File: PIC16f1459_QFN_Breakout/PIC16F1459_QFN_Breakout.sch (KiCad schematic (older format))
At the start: 9 parts, among them P1 CONN_01X05, P2 USB_OTG, P3 CONN_01X08, P4 CONN_01X08, U1 16F1459_QFN20

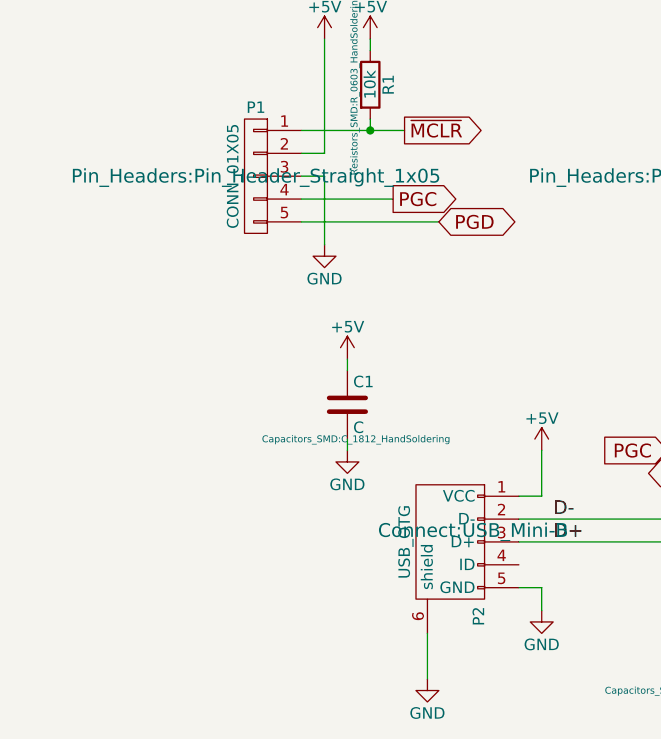
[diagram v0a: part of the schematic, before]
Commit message: Updated PIC16 breakout
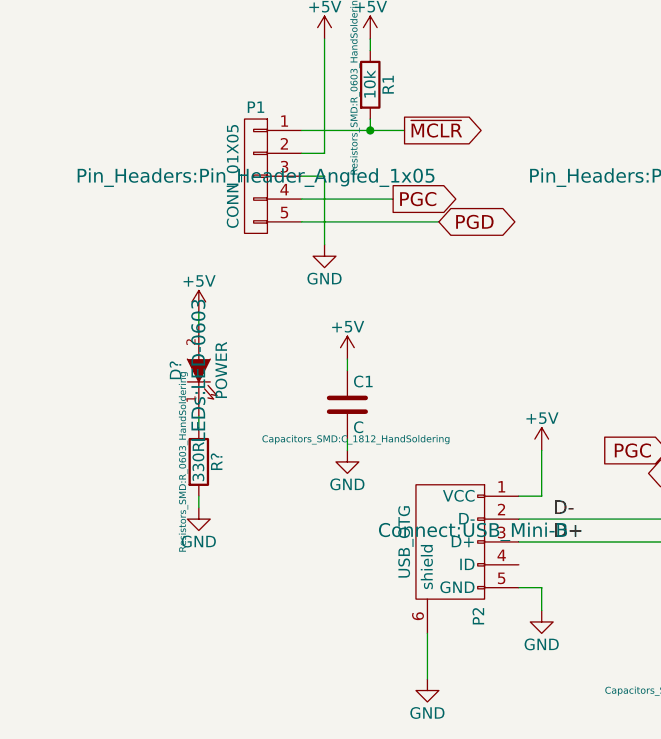
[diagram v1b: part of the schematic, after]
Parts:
- added D?: POWER, LEDs:LED-0603, symbol LED
- added R?: 330R, Resistors_SMD:R_0603_HandSoldering, symbol R
- P1: footprint Pin_Headers:Pin_Header_Straight_1x05 -> Pin_Headers:Pin_Header_Angled_1x05
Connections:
- net +5V: now also D?.2 (A)
- net GND: now also R?.2
- new net: D?.1 (K), R?.1
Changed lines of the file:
@@
 F 0 "P1" H 1050 1750 50  0000 C CNN
 F 1 "CONN_01X05" V 1150 1450 50  0000 C CNN
-F 2 "Pin_Headers:Pin_Header_Straight_1x05" H 1050 1450 60  0000 C CNN
+F 2 "Pin_Headers:Pin_Header_Angled_1x05" H 1050 1450 60  0000 C CNN
 F 3 "" H 1050 1450 60  0000 C CNN
 	1    1050 1450
@@
 Wire Wire Line
 	5450 2550 5450 1300
+$Comp
+L R R?
+U 1 1 565B9800
+P 800 2700
+F 0 "R?" V 880 2700 50  0000 C CNN
+F 1 "330R" V 800 2700 50  0000 C CNN
+F 2 "Resistors_SMD:R_0603_HandSoldering" V 730 2700 30  0000 C CNN
+F 3 "" H 800 2700 30  0000 C CNN
+	1    800  2700
+	1    0    0    -1
+$EndComp
+$Comp
+L GND #PWR?
+U 1 1 565B9870
+P 800 2900
+F 0 "#PWR?" H 800 2650 50  0001 C CNN
+F 1 "GND" H 800 2750 50  0000 C CNN
+F 2 "" H 800 2900 60  0000 C CNN
+F 3 "" H 800 2900 60  0000 C CNN
+	1    800  2900
+	1    0    0    -1
+$EndComp
+$Comp
+L +5V #PWR?
+U 1 1 565B9899
+P 800 2050
+F 0 "#PWR?" H 800 1900 50  0001 C CNN
+F 1 "+5V" H 800 2190 50  0000 C CNN
+F 2 "" H 800 2050 60  0000 C CNN
+F 3 "" H 800 2050 60  0000 C CNN
+	1    800  2050
+	1    0    0    -1
+$EndComp
+$Comp
+L LED D?
+U 1 1 565B98BA
+P 800 2300
+F 0 "D?" H 800 2400 50  0000 C CNN
+F 1 "POWER" H 800 2200 50  0000 C CNN
+F 2 "LEDs:LED-0603" H 800 2300 60  0000 C CNN
+F 3 "" H 800 2300 60  0000 C CNN
+	1    800  2300
+	0    -1   -1   0
+$EndComp
+Wire Wire Line
+	800  2900 800  2850
+Wire Wire Line
+	800  2550 800  2500
+Wire Wire Line
+	800  2100 800  2050
 $EndSCHEMATC

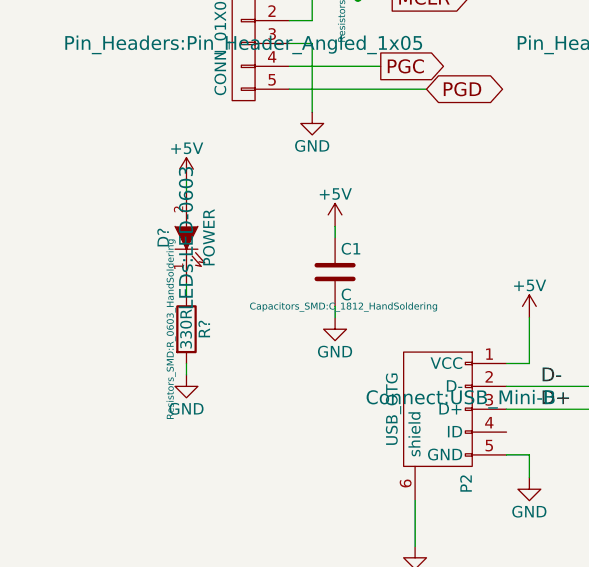
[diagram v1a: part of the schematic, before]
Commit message: Updated PIC16 breakout
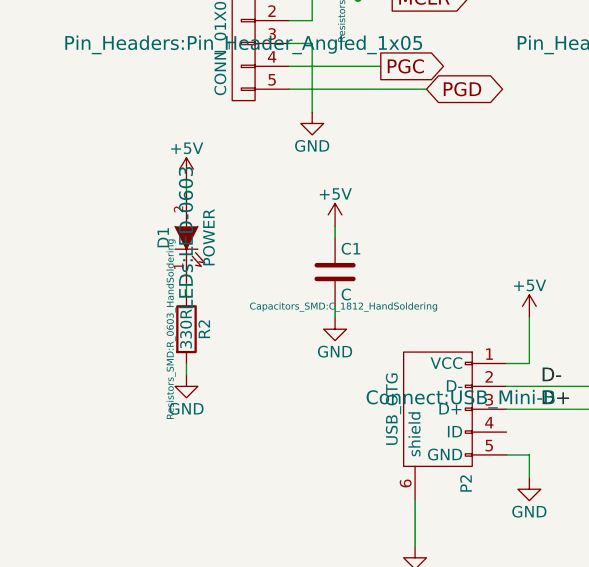
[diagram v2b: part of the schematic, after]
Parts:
- gave numbers to parts that had none: 2
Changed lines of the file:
@@
 $EndComp
 $Comp
-L GND #PWR01
+L GND #PWR10
 U 1 1 565AF913
 P 2300 3350
-F 0 "#PWR01" H 2300 3100 50  0001 C CNN
+F 0 "#PWR10" H 2300 3100 50  0001 C CNN
 F 1 "GND" H 2300 3200 50  0000 C CNN
 F 2 "" H 2300 3350 60  0000 C CNN
@@
 $EndComp
 $Comp
-L GND #PWR02
+L GND #PWR8
 U 1 1 565AF928
 P 1800 3650
-F 0 "#PWR02" H 1800 3400 50  0001 C CNN
+F 0 "#PWR8" H 1800 3400 50  0001 C CNN
 F 1 "GND" H 1800 3500 50  0000 C CNN
 F 2 "" H 1800 3650 60  0000 C CNN
@@
 $EndComp
 $Comp
-L +5V #PWR03
+L +5V #PWR9
 U 1 1 565AF95A
 P 2300 2650
-F 0 "#PWR03" H 2300 2500 50  0001 C CNN
+F 0 "#PWR9" H 2300 2500 50  0001 C CNN
 F 1 "+5V" H 2300 2790 50  0000 C CNN
 F 2 "" H 2300 2650 60  0000 C CNN
@@
 $EndComp
 $Comp
-L +5V #PWR04
+L +5V #PWR5
 U 1 1 565AF970
 P 1450 2250
-F 0 "#PWR04" H 1450 2100 50  0001 C CNN
+F 0 "#PWR5" H 1450 2100 50  0001 C CNN
 F 1 "+5V" H 1450 2390 50  0000 C CNN
 F 2 "" H 1450 2250 60  0000 C CNN
@@
 $EndComp
 $Comp
-L GND #PWR05
+L GND #PWR6
 U 1 1 565AF97E
 P 1450 2650
-F 0 "#PWR05" H 1450 2400 50  0001 C CNN
+F 0 "#PWR6" H 1450 2400 50  0001 C CNN
 F 1 "GND" H 1450 2500 50  0000 C CNN
 F 2 "" H 1450 2650 60  0000 C CNN
@@
 $EndComp
 $Comp
-L +5V #PWR06
+L +5V #PWR3
 U 1 1 565AFBB5
 P 1350 850
-F 0 "#PWR06" H 1350 700 50  0001 C CNN
+F 0 "#PWR3" H 1350 700 50  0001 C CNN
 F 1 "+5V" H 1350 990 50  0000 C CNN
 F 2 "" H 1350 850 60  0000 C CNN
@@
 $EndComp
 $Comp
-L GND #PWR07
+L GND #PWR4
 U 1 1 565AFBDC
 P 1350 1750
-F 0 "#PWR07" H 1350 1500 50  0001 C CNN
+F 0 "#PWR4" H 1350 1500 50  0001 C CNN
 F 1 "GND" H 1350 1600 50  0000 C CNN
 F 2 "" H 1350 1750 60  0000 C CNN
@@
 ~MCLR
 $Comp
-L +5V #PWR08
+L +5V #PWR7
 U 1 1 565AFC9F
 P 1550 850
-F 0 "#PWR08" H 1550 700 50  0001 C CNN
+F 0 "#PWR7" H 1550 700 50  0001 C CNN
 F 1 "+5V" H 1550 990 50  0000 C CNN
 F 2 "" H 1550 850 60  0000 C CNN
@@
 $EndComp
 $Comp
-L GND #PWR09
+L GND #PWR11
 U 1 1 565B07D7
 P 2950 3900
-F 0 "#PWR09" H 2950 3650 50  0001 C CNN
+F 0 "#PWR11" H 2950 3650 50  0001 C CNN
 F 1 "GND" H 2950 3750 50  0000 C CNN
 F 2 "" H 2950 3900 60  0000 C CNN
@@
 $EndComp
 $Comp
-L GND #PWR010
+L GND #PWR12
 U 1 1 565B084A
 P 3200 4200
-F 0 "#PWR010" H 3200 3950 50  0001 C CNN
+F 0 "#PWR12" H 3200 3950 50  0001 C CNN
 F 1 "GND" H 3200 4050 50  0000 C CNN
 F 2 "" H 3200 4200 60  0000 C CNN
@@
 $EndComp
 $Comp
-L GND #PWR011
+L GND #PWR14
 U 1 1 565B086A
 P 3350 4200
-F 0 "#PWR011" H 3350 3950 50  0001 C CNN
+F 0 "#PWR14" H 3350 3950 50  0001 C CNN
 F 1 "GND" H 3350 4050 50  0000 C CNN
 F 2 "" H 3350 4200 60  0000 C CNN
@@
 $EndComp
 $Comp
-L +5V #PWR012
+L +5V #PWR13
 U 1 1 565B08FC
 P 3350 2300
-F 0 "#PWR012" H 3350 2150 50  0001 C CNN
+F 0 "#PWR13" H 3350 2150 50  0001 C CNN
 F 1 "+5V" H 3350 2440 50  0000 C CNN
 F 2 "" H 3350 2300 60  0000 C CNN
@@
 $EndComp
 $Comp
-L +5V #PWR013
+L +5V #PWR15
 U 1 1 565B0AE2
 P 4500 1000
-F 0 "#PWR013" H 4500 850 50  0001 C CNN
+F 0 "#PWR15" H 4500 850 50  0001 C CNN
 F 1 "+5V" H 4500 1140 50  0000 C CNN
 F 2 "" H 4500 1000 60  0000 C CNN
@@
 $EndComp
 $Comp
-L GND #PWR014
+L GND #PWR16
 U 1 1 565B0BF7
 P 4500 1300
-F 0 "#PWR014" H 4500 1050 50  0001 C CNN
+F 0 "#PWR16" H 4500 1050 50  0001 C CNN
 F 1 "GND" H 4500 1150 50  0000 C CNN
 F 2 "" H 4500 1300 60  0000 C CNN
@@
 	5450 2550 5450 1300
 $Comp
-L R R?
+L R R2
 U 1 1 565B9800
 P 800 2700
-F 0 "R?" V 880 2700 50  0000 C CNN
+F 0 "R2" V 880 2700 50  0000 C CNN
 F 1 "330R" V 800 2700 50  0000 C CNN
 F 2 "Resistors_SMD:R_0603_HandSoldering" V 730 2700 30  0000 C CNN
@@
 $EndComp
 $Comp
-L GND #PWR?
+L GND #PWR2
 U 1 1 565B9870
 P 800 2900
-F 0 "#PWR?" H 800 2650 50  0001 C CNN
+F 0 "#PWR2" H 800 2650 50  0001 C CNN
 F 1 "GND" H 800 2750 50  0000 C CNN
 F 2 "" H 800 2900 60  0000 C CNN
@@
 $EndComp
 $Comp
-L +5V #PWR?
+L +5V #PWR1
 U 1 1 565B9899
 P 800 2050
-F 0 "#PWR?" H 800 1900 50  0001 C CNN
+F 0 "#PWR1" H 800 1900 50  0001 C CNN
 F 1 "+5V" H 800 2190 50  0000 C CNN
 F 2 "" H 800 2050 60  0000 C CNN
@@
 $EndComp
 $Comp
-L LED D?
+L LED D1
 U 1 1 565B98BA
 P 800 2300
-F 0 "D?" H 800 2400 50  0000 C CNN
+F 0 "D1" H 800 2400 50  0000 C CNN
 F 1 "POWER" H 800 2200 50  0000 C CNN
 F 2 "LEDs:LED-0603" H 800 2300 60  0000 C CNN

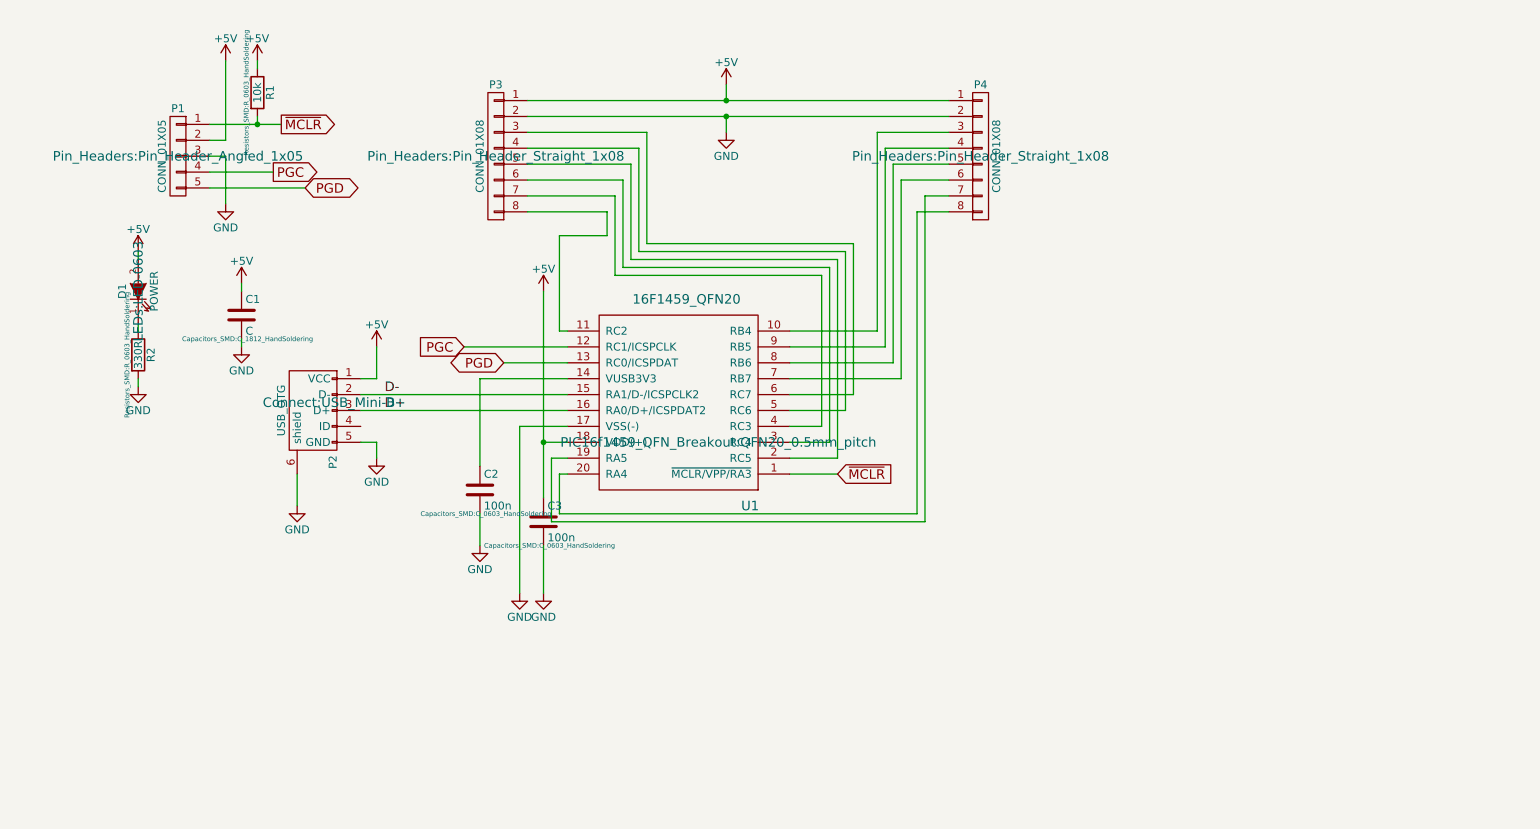
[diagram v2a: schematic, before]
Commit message: Updated PIC16 breakout
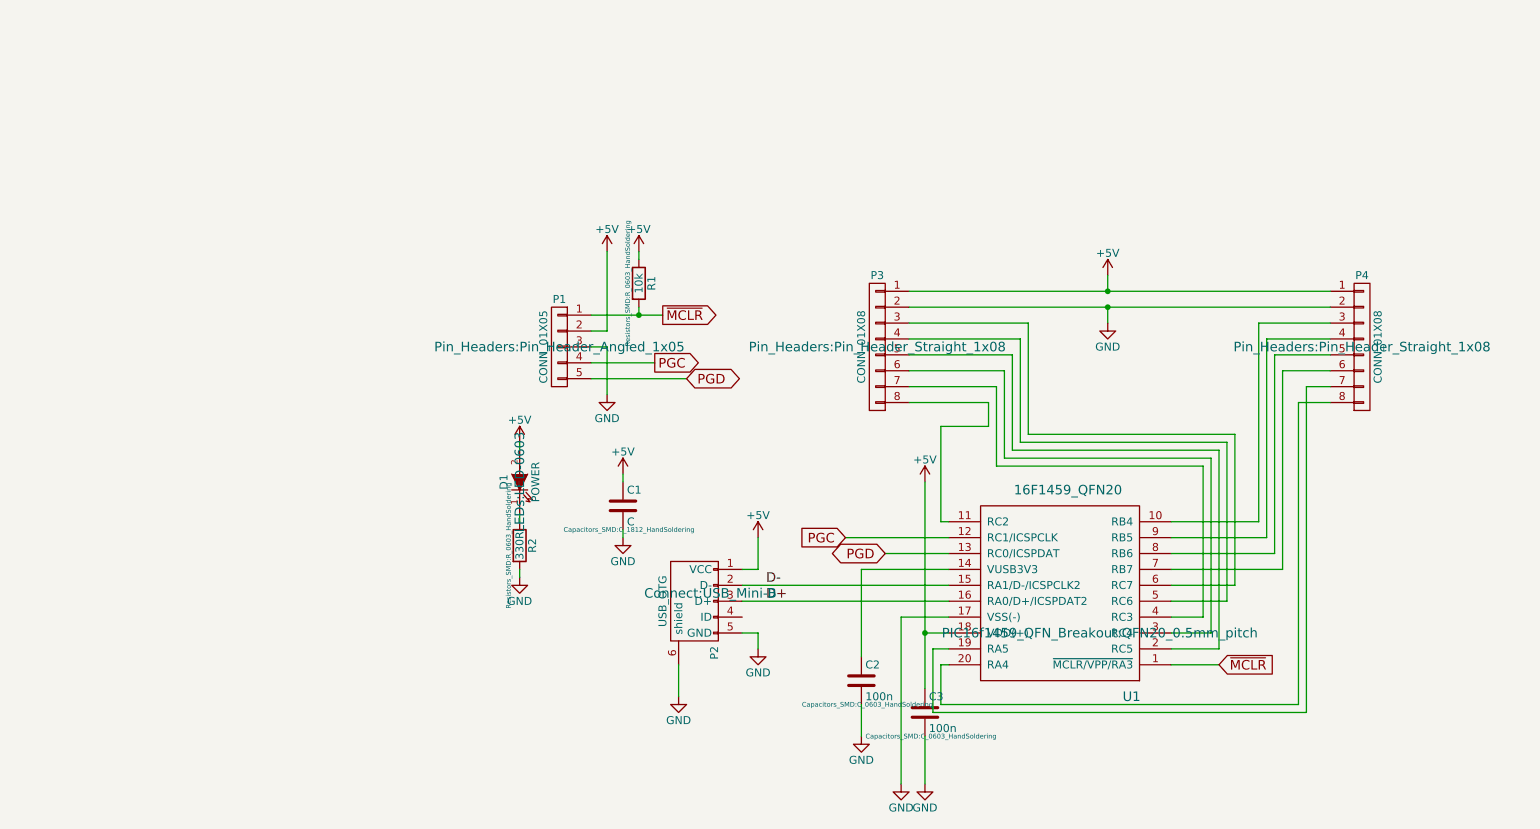
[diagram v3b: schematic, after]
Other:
- moved on the sheet: C1, C2, C3, D1, P1, P2, P3, P4, R1, R2, U1

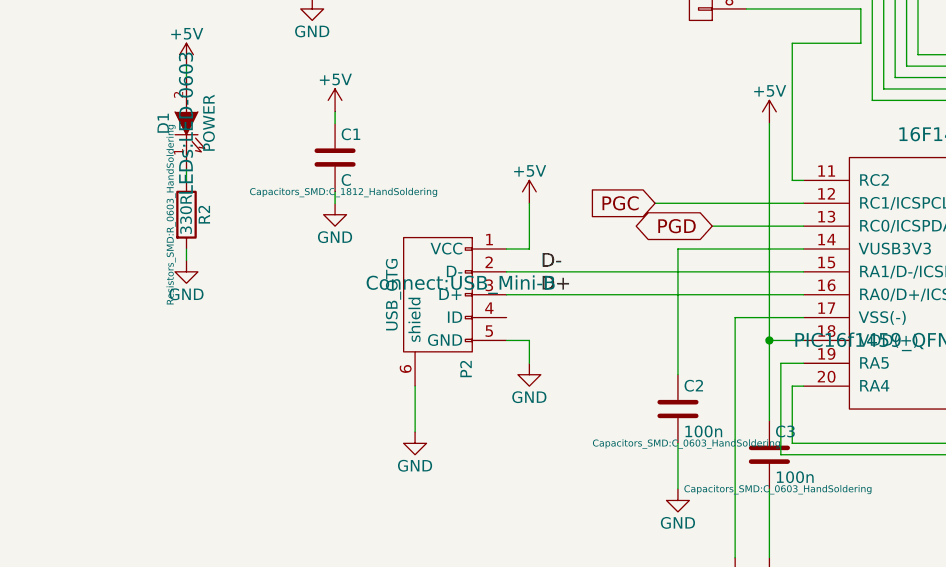
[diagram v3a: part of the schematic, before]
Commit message: Update PIC16F USB Board and PIC 24F/32 USB board
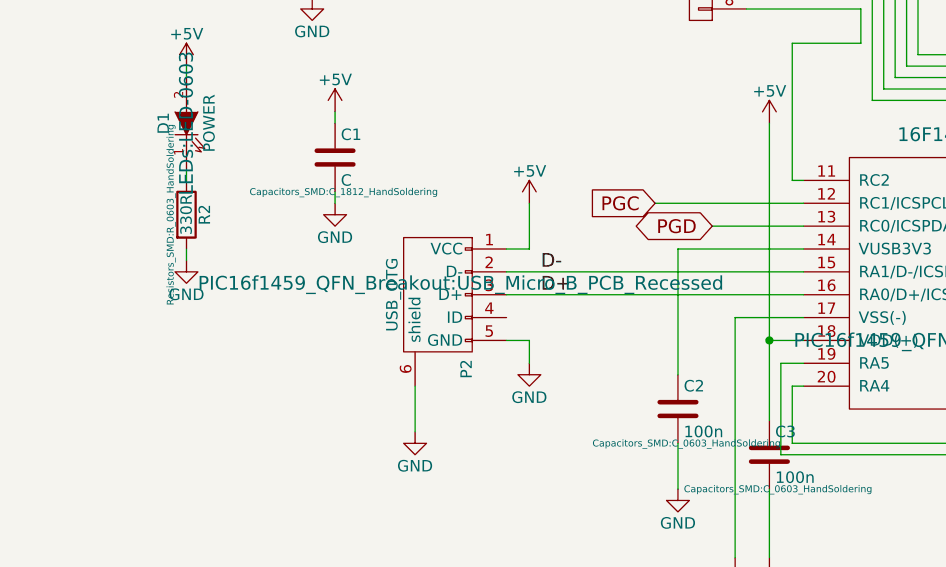
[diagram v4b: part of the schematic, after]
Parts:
- P2: footprint Connect:USB_Mini-B -> PIC16f1459_QFN_Breakout:USB_Micro_B_PCB_Recessed
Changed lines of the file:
@@
 F 0 "P2" H 4625 4125 50  0000 C CNN
 F 1 "USB_OTG" H 4300 4450 50  0000 C CNN
-F 2 "Connect:USB_Mini-B" V 4250 4150 60  0000 C CNN
+F 2 "PIC16f1459_QFN_Breakout:USB_Micro_B_PCB_Recessed" V 4250 4150 60  0000 C CNN
 F 3 "" V 4250 4150 60  0000 C CNN
 	1    4300 4250
@@
 $EndComp
 $Comp
-L GND #PWR10
+L GND #PWR01
 U 1 1 565AF913
 P 4700 4550
-F 0 "#PWR10" H 4700 4300 50  0001 C CNN
+F 0 "#PWR01" H 4700 4300 50  0001 C CNN
 F 1 "GND" H 4700 4400 50  0000 C CNN
 F 2 "" H 4700 4550 60  0000 C CNN
@@
 $EndComp
 $Comp
-L GND #PWR8
+L GND #PWR02
 U 1 1 565AF928
 P 4200 4850
-F 0 "#PWR8" H 4200 4600 50  0001 C CNN
+F 0 "#PWR02" H 4200 4600 50  0001 C CNN
 F 1 "GND" H 4200 4700 50  0000 C CNN
 F 2 "" H 4200 4850 60  0000 C CNN
@@
 $EndComp
 $Comp
-L +5V #PWR9
+L +5V #PWR03
 U 1 1 565AF95A
 P 4700 3850
-F 0 "#PWR9" H 4700 3700 50  0001 C CNN
+F 0 "#PWR03" H 4700 3700 50  0001 C CNN
 F 1 "+5V" H 4700 3990 50  0000 C CNN
 F 2 "" H 4700 3850 60  0000 C CNN
@@
 $EndComp
 $Comp
-L +5V #PWR5
+L +5V #PWR04
 U 1 1 565AF970
 P 3850 3450
-F 0 "#PWR5" H 3850 3300 50  0001 C CNN
+F 0 "#PWR04" H 3850 3300 50  0001 C CNN
 F 1 "+5V" H 3850 3590 50  0000 C CNN
 F 2 "" H 3850 3450 60  0000 C CNN
@@
 $EndComp
 $Comp
-L GND #PWR6
+L GND #PWR05
 U 1 1 565AF97E
 P 3850 3850
-F 0 "#PWR6" H 3850 3600 50  0001 C CNN
+F 0 "#PWR05" H 3850 3600 50  0001 C CNN
 F 1 "GND" H 3850 3700 50  0000 C CNN
 F 2 "" H 3850 3850 60  0000 C CNN
@@
 $EndComp
 $Comp
-L +5V #PWR3
+L +5V #PWR06
 U 1 1 565AFBB5
 P 3750 2050
-F 0 "#PWR3" H 3750 1900 50  0001 C CNN
+F 0 "#PWR06" H 3750 1900 50  0001 C CNN
 F 1 "+5V" H 3750 2190 50  0000 C CNN
 F 2 "" H 3750 2050 60  0000 C CNN
@@
 $EndComp
 $Comp
-L GND #PWR4
+L GND #PWR07
 U 1 1 565AFBDC
 P 3750 2950
-F 0 "#PWR4" H 3750 2700 50  0001 C CNN
+F 0 "#PWR07" H 3750 2700 50  0001 C CNN
 F 1 "GND" H 3750 2800 50  0000 C CNN
 F 2 "" H 3750 2950 60  0000 C CNN
@@
 ~MCLR
 $Comp
-L +5V #PWR7
+L +5V #PWR08
 U 1 1 565AFC9F
 P 3950 2050
-F 0 "#PWR7" H 3950 1900 50  0001 C CNN
+F 0 "#PWR08" H 3950 1900 50  0001 C CNN
 F 1 "+5V" H 3950 2190 50  0000 C CNN
 F 2 "" H 3950 2050 60  0000 C CNN
@@
 $EndComp
 $Comp
-L GND #PWR11
+L GND #PWR09
 U 1 1 565B07D7
 P 5350 5100
-F 0 "#PWR11" H 5350 4850 50  0001 C CNN
+F 0 "#PWR09" H 5350 4850 50  0001 C CNN
 F 1 "GND" H 5350 4950 50  0000 C CNN
 F 2 "" H 5350 5100 60  0000 C CNN
@@
 $EndComp
 $Comp
-L GND #PWR12
+L GND #PWR010
 U 1 1 565B084A
 P 5600 5400
-F 0 "#PWR12" H 5600 5150 50  0001 C CNN
+F 0 "#PWR010" H 5600 5150 50  0001 C CNN
 F 1 "GND" H 5600 5250 50  0000 C CNN
 F 2 "" H 5600 5400 60  0000 C CNN
@@
 $EndComp
 $Comp
-L GND #PWR14
+L GND #PWR011
 U 1 1 565B086A
 P 5750 5400
-F 0 "#PWR14" H 5750 5150 50  0001 C CNN
+F 0 "#PWR011" H 5750 5150 50  0001 C CNN
 F 1 "GND" H 5750 5250 50  0000 C CNN
 F 2 "" H 5750 5400 60  0000 C CNN
@@
 $EndComp
 $Comp
-L +5V #PWR13
+L +5V #PWR012
 U 1 1 565B08FC
 P 5750 3500
-F 0 "#PWR13" H 5750 3350 50  0001 C CNN
+F 0 "#PWR012" H 5750 3350 50  0001 C CNN
 F 1 "+5V" H 5750 3640 50  0000 C CNN
 F 2 "" H 5750 3500 60  0000 C CNN
@@
 $EndComp
 $Comp
-L +5V #PWR15
+L +5V #PWR013
 U 1 1 565B0AE2
 P 6900 2200
-F 0 "#PWR15" H 6900 2050 50  0001 C CNN
+F 0 "#PWR013" H 6900 2050 50  0001 C CNN
 F 1 "+5V" H 6900 2340 50  0000 C CNN
 F 2 "" H 6900 2200 60  0000 C CNN
@@
 $EndComp
 $Comp
-L GND #PWR16
+L GND #PWR014
 U 1 1 565B0BF7
 P 6900 2500
-F 0 "#PWR16" H 6900 2250 50  0001 C CNN
+F 0 "#PWR014" H 6900 2250 50  0001 C CNN
 F 1 "GND" H 6900 2350 50  0000 C CNN
 F 2 "" H 6900 2500 60  0000 C CNN
@@
 $EndComp
 $Comp
-L GND #PWR2
+L GND #PWR015
 U 1 1 565B9870
 P 3200 4100
-F 0 "#PWR2" H 3200 3850 50  0001 C CNN
+F 0 "#PWR015" H 3200 3850 50  0001 C CNN
 F 1 "GND" H 3200 3950 50  0000 C CNN
 F 2 "" H 3200 4100 60  0000 C CNN
@@
 $EndComp
 $Comp
-L +5V #PWR1
+L +5V #PWR016
 U 1 1 565B9899
 P 3200 3250
-F 0 "#PWR1" H 3200 3100 50  0001 C CNN
+F 0 "#PWR016" H 3200 3100 50  0001 C CNN
 F 1 "+5V" H 3200 3390 50  0000 C CNN
 F 2 "" H 3200 3250 60  0000 C CNN
